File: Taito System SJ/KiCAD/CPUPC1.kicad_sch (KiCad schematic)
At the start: 44 parts, among them U11 74LS161, U13 74LS161, U17 74LS85, U18 74LS85, U19 74LS85, U21 74LS04, U24 74LS161, U26 74LS161, U34 74LS08, U36 74LS04, U37 74LS164, U38 74LS175, U51 74LS74, U61 74LS02, U62 74LS00, U63 74LS367, U74 74LS74, U75 74LS74, U88 74LS04, U94 74LS32, U97 74LS74

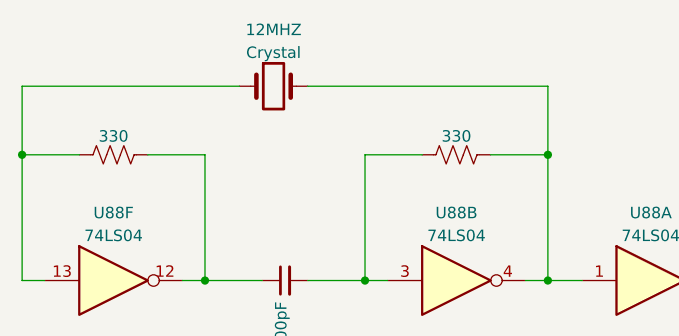
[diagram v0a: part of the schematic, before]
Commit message: Added CPU
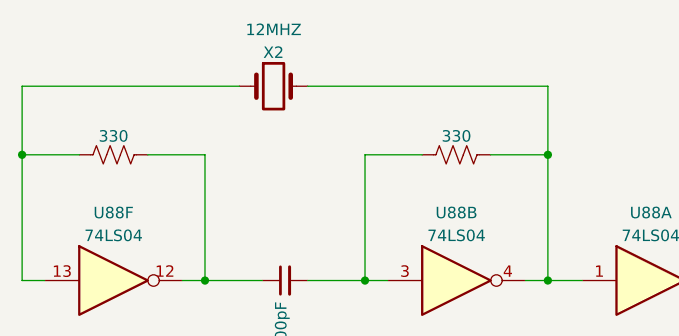
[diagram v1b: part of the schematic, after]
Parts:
- 12MHZ: value Crystal -> X2
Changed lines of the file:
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@@
     (in_bom yes) (on_board yes) (fields_autoplaced)
     (property "Reference" "12MHZ" (id 0) (at 50.8 20.4048 0))
-    (property "Value" "Crystal" (id 1) (at 50.8 22.9417 0))
+    (property "Value" "X2" (id 1) (at 50.8 22.9417 0))
     (property "Footprint" "" (id 2) (at 50.8 26.67 0)
       (effects (font (size 1.27 1.27)) hide)
